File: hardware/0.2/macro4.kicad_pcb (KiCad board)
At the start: 2 copper layers, 48 x 48 mm, 29 parts, among them J1 USB_C_Receptacle_USB2.0, Q1 BSS138, SW1 SIDE, SW2 SIDE, SW3 CHERRY_MX, SW5 CHERRY_MX, SW6 CHERRY_MX, SW7 Rotary_Encoder_MX, U1 AP2112K-3.3, U2 STM32F072C8Tx

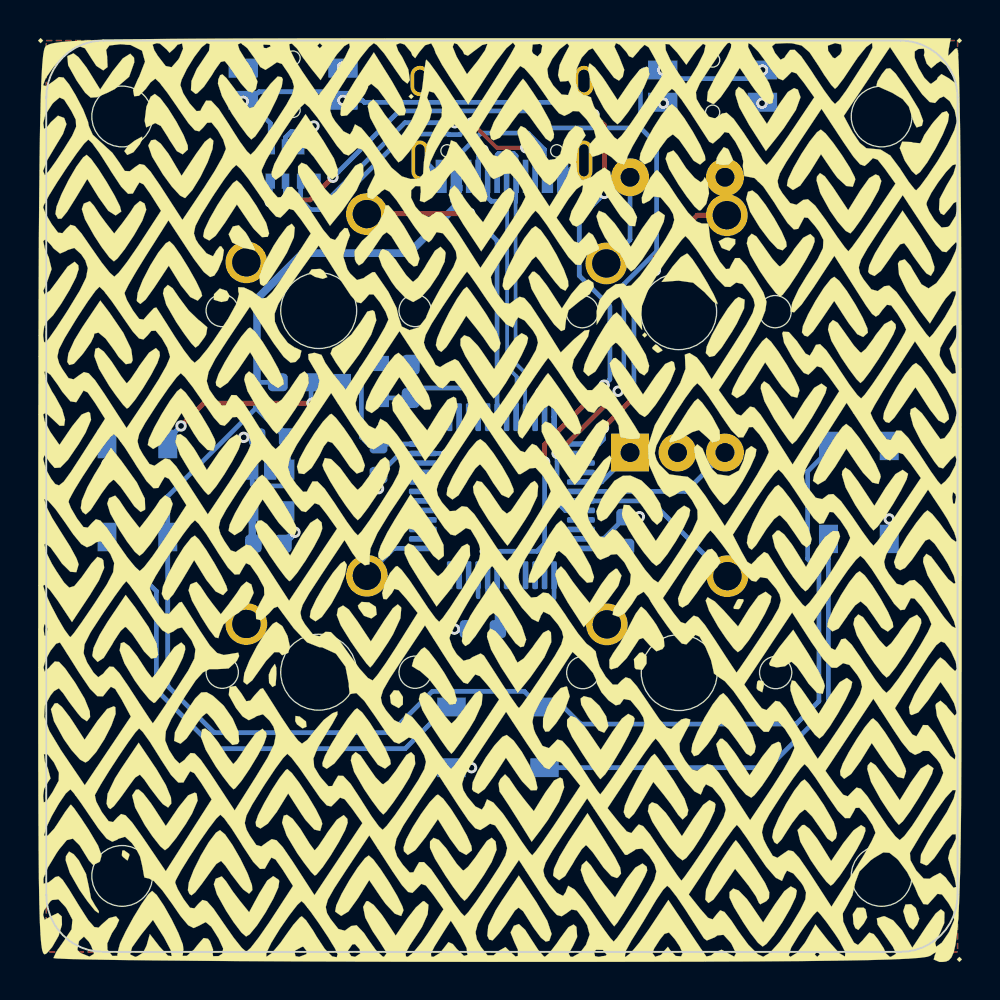
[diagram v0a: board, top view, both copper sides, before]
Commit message: added second encoder, fixed panelisation script
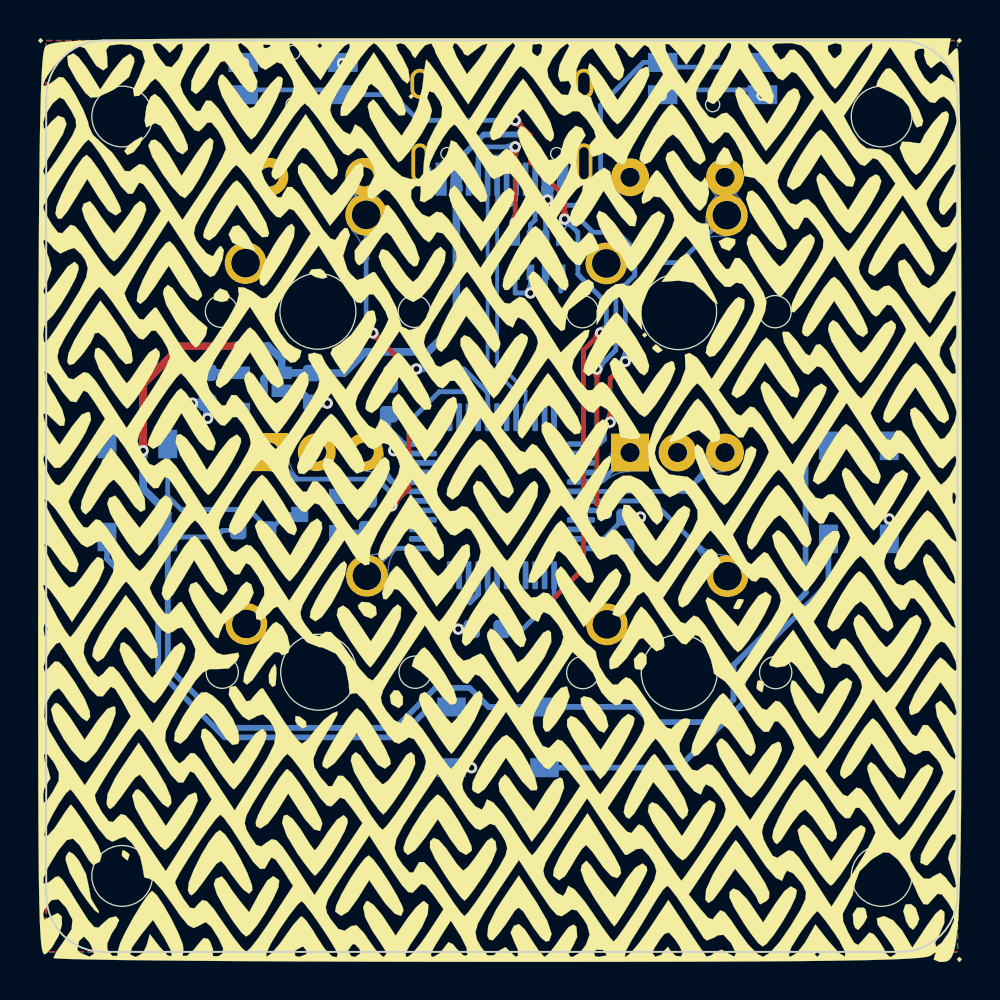
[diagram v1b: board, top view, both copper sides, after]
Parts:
- removed SW6: CHERRY_MX, josh-keyboard:MX_KEYSWITCH
- added SW4: Rotary_Encoder_MX, josh-keyboard:MX_KEYSWITCH_ENCODER, F.Cu at (68.2, 102.3)
- LOGO1: footprint josh-logos:josh-johnson-logo-11x2 -> josh-logos:josh-johnson-logo-17x3
- R1, R2: footprint Resistor_SMD:R_0603_1608Metric_Pad1.05x0.95mm_HandSolder -> Resistor_SMD:R_0603_1608Metric
- moved RN1 13.8 mm to (79.9, 99.3), turned to 90 degrees
- moved C3 8.81 mm to (62.5, 106.3), turned to 90 degrees
- moved R2 8.10 mm to (64.9, 113.8)
- moved Q1 7.35 mm to (68.3, 113.0)
- moved R1 7.35 mm to (71.0, 113.0)
- moved U1 5.27 mm to (65.3, 106.5), turned to 180 degrees
- moved C1 3.34 mm to (68.0, 106.3), turned to 90 degrees
- moved C4 3.25 mm to (72.0, 106.9), turned to 90 degrees
- moved LOGO3 2.20 mm to (66.6, 131.4)
- moved LOGO1 1.36 mm to (78.8, 129.5)
- moved SW1 0.40 mm to (89.1, 90.0)
- moved SW2 0.30 mm to (67.0, 90.0)
- moved C2 0.20 mm to (77.2, 119.0)
- moved LOGO2 0.20 mm to (80.1, 131.8)
- moved J1 0.15 mm to (78.0, 92.2)
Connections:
- net /ENC_A renamed /ENC_1_A
- net /ENC_B renamed /ENC_1_B
- D3 pad 2: Net-(D3-Pad2) -> (no net)
- J1 pad A8: Net-(J1-PadA8) -> (no net)
- J1 pad B8: Net-(J1-PadB8) -> (no net)
- RN1 pad 1: /nRST -> +3V3
- RN1 pad 8: +3V3 -> /nRST
- SW7 pad S1: /KEY_2 -> /KEY_1
- U1 pad 4: Net-(U1-Pad4) -> (no net)
- U2 pad 10: Net-(U2-Pad10) -> (no net)
- U2 pad 11: Net-(U2-Pad11) -> (no net)
- U2 pad 12: Net-(U2-Pad12) -> (no net)
- U2 pad 14: Net-(U2-Pad14) -> (no net)
- U2 pad 15: Net-(U2-Pad15) -> (no net)
- U2 pad 16: Net-(U2-Pad16) -> (no net)
- U2 pad 17: Net-(U2-Pad17) -> (no net)
- U2 pad 18: Net-(U2-Pad18) -> (no net)
- U2 pad 19: Net-(U2-Pad19) -> /ENC_2_A
- U2 pad 2: Net-(U2-Pad2) -> (no net)
- U2 pad 20: Net-(U2-Pad20) -> /ENC_2_B
- U2 pad 21: Net-(U2-Pad21) -> (no net)
- U2 pad 22: Net-(U2-Pad22) -> (no net)
- U2 pad 25: Net-(U2-Pad25) -> (no net)
- U2 pad 26: Net-(U2-Pad26) -> (no net)
- U2 pad 27: Net-(U2-Pad27) -> (no net)
- U2 pad 29: Net-(U2-Pad29) -> /KEY_2
- U2 pad 3: Net-(U2-Pad3) -> (no net)
- U2 pad 30: /KEY_1 -> (no net)
- U2 pad 31: Net-(U2-Pad31) -> (no net)
- U2 pad 34: Net-(U2-Pad34) -> (no net)
- U2 pad 37: /KEY_2 -> /KEY_1
- U2 pad 38: Net-(U2-Pad38) -> (no net)
- U2 pad 39: Net-(U2-Pad39) -> (no net)
- U2 pad 4: Net-(U2-Pad4) -> (no net)
- U2 pad 40: Net-(U2-Pad40) -> (no net)
- U2 pad 45: Net-(U2-Pad45) -> (no net)
- U2 pad 46: Net-(U2-Pad46) -> (no net)
- U2 pad 5: Net-(U2-Pad5) -> (no net)
- U2 pad 6: Net-(U2-Pad6) -> (no net)
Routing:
- net /BOOT0: track 55.4 -> 39.0 mm, vias 6 -> 2
- net Net-(J1-PadB5): track 17.3 -> 3.30 mm, vias 2 -> 0
- net GND: track 35.1 -> 24.5 mm, vias 14 -> 15
- net /ENC_2_A: track 0.00 -> 8.94 mm
- net /LED: track 6.64 -> 13.7 mm, vias 0 -> 2
- net Net-(J1-PadA5): track 13.5 -> 8.34 mm
- net VBUS: track 106.0 -> 110.1 mm, vias 0 -> 4
- net /ENC_2_B: track 0.00 -> 3.79 mm
- net /nRST: track 54.7 -> 51.0 mm, vias 6 -> 4
- net Net-(D2-Pad2): track 25.1 -> 22.4 mm
- net +3V3: track 18.5 -> 21.1 mm, vias 3 -> 2
- net /KEY_2: track 18.7 -> 17.0 mm, vias 3 -> 2
- net /KEY_1: track 16.8 -> 18.5 mm, vias 1 -> 2
- net /USB_D-: track 15.1 -> 16.4 mm
- net Net-(D1-Pad2): track 26.9 -> 25.7 mm
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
